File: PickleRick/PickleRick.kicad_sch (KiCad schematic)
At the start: 83 parts, among them J1 Conn_01x06_Male, J10 Conn_01x03_Male, J11 Conn_01x02_Male, J2 Conn_01x02_Male, J3 Conn_01x02_Male, J4 Micro_SD_Card_Det, J5 292227-7, Q1 MMDT2222A, Q2 PMV20ENR, U1 SN65HVD230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

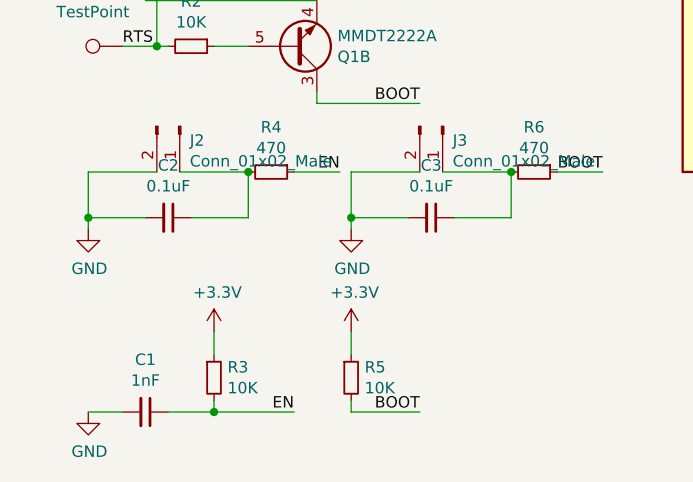
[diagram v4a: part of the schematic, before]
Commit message: changed autoprogrammer cap values
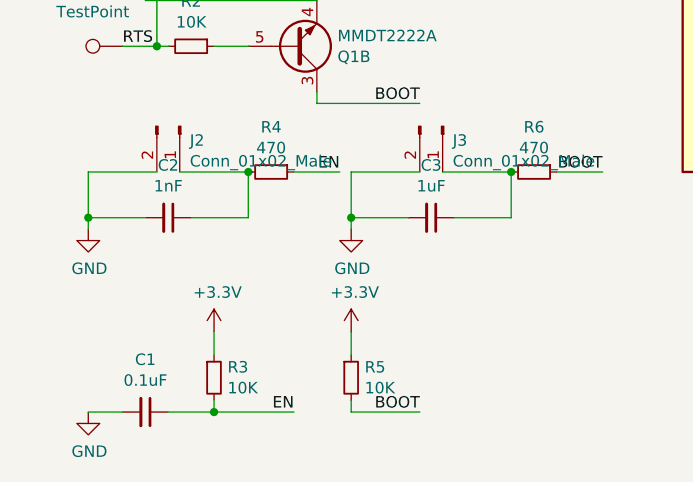
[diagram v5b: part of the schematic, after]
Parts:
- C1: value 1nF -> 0.1uF
- C2: value 0.1uF -> 1nF
- C3: value 0.1uF -> 1uF
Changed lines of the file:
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@@
     (in_bom yes) (on_board yes)
     (property "Reference" "C1" (id 0) (at 22.86 185.9534 90))
-    (property "Value" "1nF" (id 1) (at 22.86 188.2648 90))
+    (property "Value" "0.1uF" (id 1) (at 22.86 188.2648 90))
     (property "Footprint" "Capacitor_SMD:C_0603_1608Metric" (id 2) (at 22.86 191.77 0)
       (effects (font (size 1.27 1.27)) hide)
@@
     (in_bom yes) (on_board yes)
     (property "Reference" "C2" (id 0) (at 25.4 164.3634 90))
-    (property "Value" "0.1uF" (id 1) (at 25.4 166.6748 90))
+    (property "Value" "1nF" (id 1) (at 25.4 166.6748 90))
     (property "Footprint" "Capacitor_SMD:C_0603_1608Metric" (id 2) (at 25.4 170.18 0)
       (effects (font (size 1.27 1.27)) hide)
@@
     (in_bom yes) (on_board yes)
     (property "Reference" "C3" (id 0) (at 54.61 164.3634 90))
-    (property "Value" "0.1uF" (id 1) (at 54.61 166.6748 90))
+    (property "Value" "1uF" (id 1) (at 54.61 166.6748 90))
     (property "Footprint" "Capacitor_SMD:C_0603_1608Metric" (id 2) (at 54.61 170.18 0)
       (effects (font (size 1.27 1.27)) hide)
@@
     (path "/ca0eab8e-e3fd-464d-bb03-d1603b8a651b" (page "3"))
     (path "/7b7fe22f-5db7-4fb0-a6e2-91b9a8e5f484" (page "4"))
-    (path "/150d7a0e-7d8c-4788-bc30-4a3682bf4d09" (page "7"))
     (path "/53a382a5-9123-45f3-a2e9-3b2de6ca541d" (page "5"))
     (path "/698a410d-6a39-45b6-9e32-be9222181ad1" (page "7"))
+    (path "/150d7a0e-7d8c-4788-bc30-4a3682bf4d09" (page "7"))
     (path "/a5e505c0-c0af-4f61-a9d4-cf031c548012" (page "7"))
   )
@@
     )
     (path "/3bef0362-242d-46c4-b651-9d41a3c29516"
-      (reference "C1") (unit 1) (value "1nF") (footprint "Capacitor_SMD:C_0603_1608Metric")
+      (reference "C1") (unit 1) (value "0.1uF") (footprint "Capacitor_SMD:C_0603_1608Metric")
     )
     (path "/8f141cb6-d196-4940-89f8-4e8940598ec7"
-      (reference "C2") (unit 1) (value "0.1uF") (footprint "Capacitor_SMD:C_0603_1608Metric")
+      (reference "C2") (unit 1) (value "1nF") (footprint "Capacitor_SMD:C_0603_1608Metric")
     )
     (path "/d2eb360b-2bc4-4408-a8b3-07959277e262"
-      (reference "C3") (unit 1) (value "0.1uF") (footprint "Capacitor_SMD:C_0603_1608Metric")
+      (reference "C3") (unit 1) (value "1uF") (footprint "Capacitor_SMD:C_0603_1608Metric")
     )
     (path "/f238640e-3401-420a-ac31-a433f268cbfc"

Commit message: final changes to pick rick
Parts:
- C2: value 1nF -> 0.1uF
- C3: value 1uF -> 0.1uF
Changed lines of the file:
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@@
     (in_bom yes) (on_board yes)
     (property "Reference" "C2" (id 0) (at 25.4 164.3634 90))
-    (property "Value" "1nF" (id 1) (at 25.4 166.6748 90))
+    (property "Value" "0.1uF" (id 1) (at 25.4 166.6748 90))
     (property "Footprint" "Capacitor_SMD:C_0603_1608Metric" (id 2) (at 25.4 170.18 0)
       (effects (font (size 1.27 1.27)) hide)
@@
     (in_bom yes) (on_board yes)
     (property "Reference" "C3" (id 0) (at 54.61 164.3634 90))
-    (property "Value" "1uF" (id 1) (at 54.61 166.6748 90))
+    (property "Value" "0.1uF" (id 1) (at 54.61 166.6748 90))
     (property "Footprint" "Capacitor_SMD:C_0603_1608Metric" (id 2) (at 54.61 170.18 0)
       (effects (font (size 1.27 1.27)) hide)
@@
     (path "/ca0eab8e-e3fd-464d-bb03-d1603b8a651b" (page "3"))
     (path "/7b7fe22f-5db7-4fb0-a6e2-91b9a8e5f484" (page "4"))
+    (path "/150d7a0e-7d8c-4788-bc30-4a3682bf4d09" (page "7"))
     (path "/53a382a5-9123-45f3-a2e9-3b2de6ca541d" (page "5"))
     (path "/698a410d-6a39-45b6-9e32-be9222181ad1" (page "7"))
-    (path "/150d7a0e-7d8c-4788-bc30-4a3682bf4d09" (page "7"))
     (path "/a5e505c0-c0af-4f61-a9d4-cf031c548012" (page "7"))
   )
@@
     )
     (path "/8f141cb6-d196-4940-89f8-4e8940598ec7"
-      (reference "C2") (unit 1) (value "1nF") (footprint "Capacitor_SMD:C_0603_1608Metric")
+      (reference "C2") (unit 1) (value "0.1uF") (footprint "Capacitor_SMD:C_0603_1608Metric")
     )
     (path "/d2eb360b-2bc4-4408-a8b3-07959277e262"
-      (reference "C3") (unit 1) (value "1uF") (footprint "Capacitor_SMD:C_0603_1608Metric")
+      (reference "C3") (unit 1) (value "0.1uF") (footprint "Capacitor_SMD:C_0603_1608Metric")
     )
     (path "/f238640e-3401-420a-ac31-a433f268cbfc"

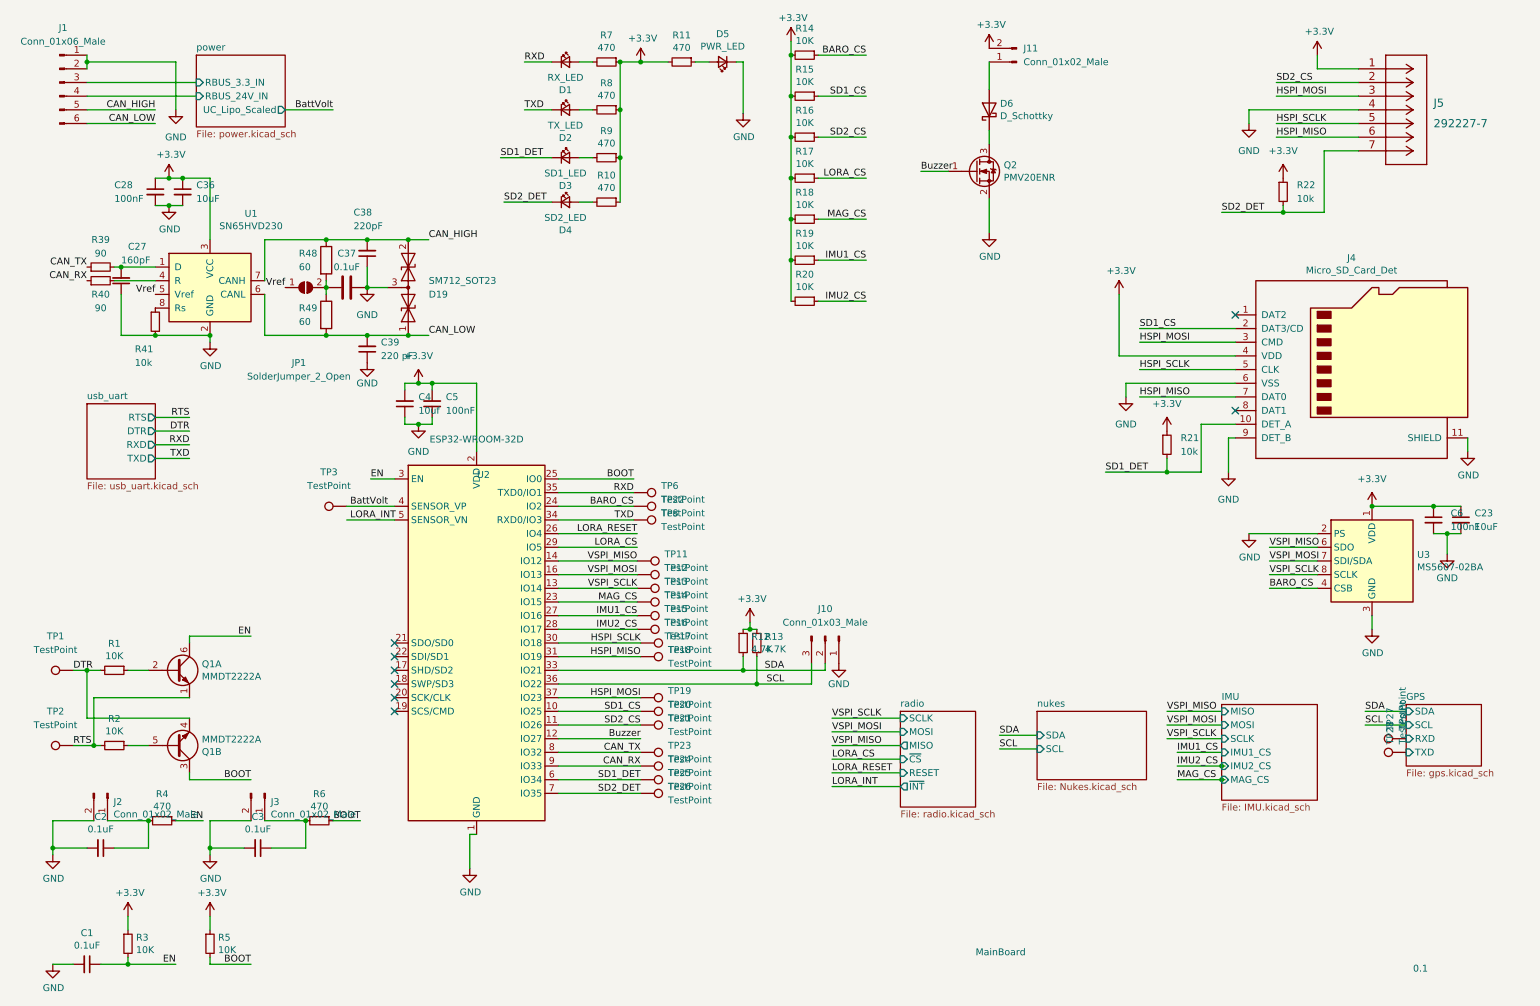
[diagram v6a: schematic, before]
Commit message: switched vspi and hspi labels so they are consistent with documentation
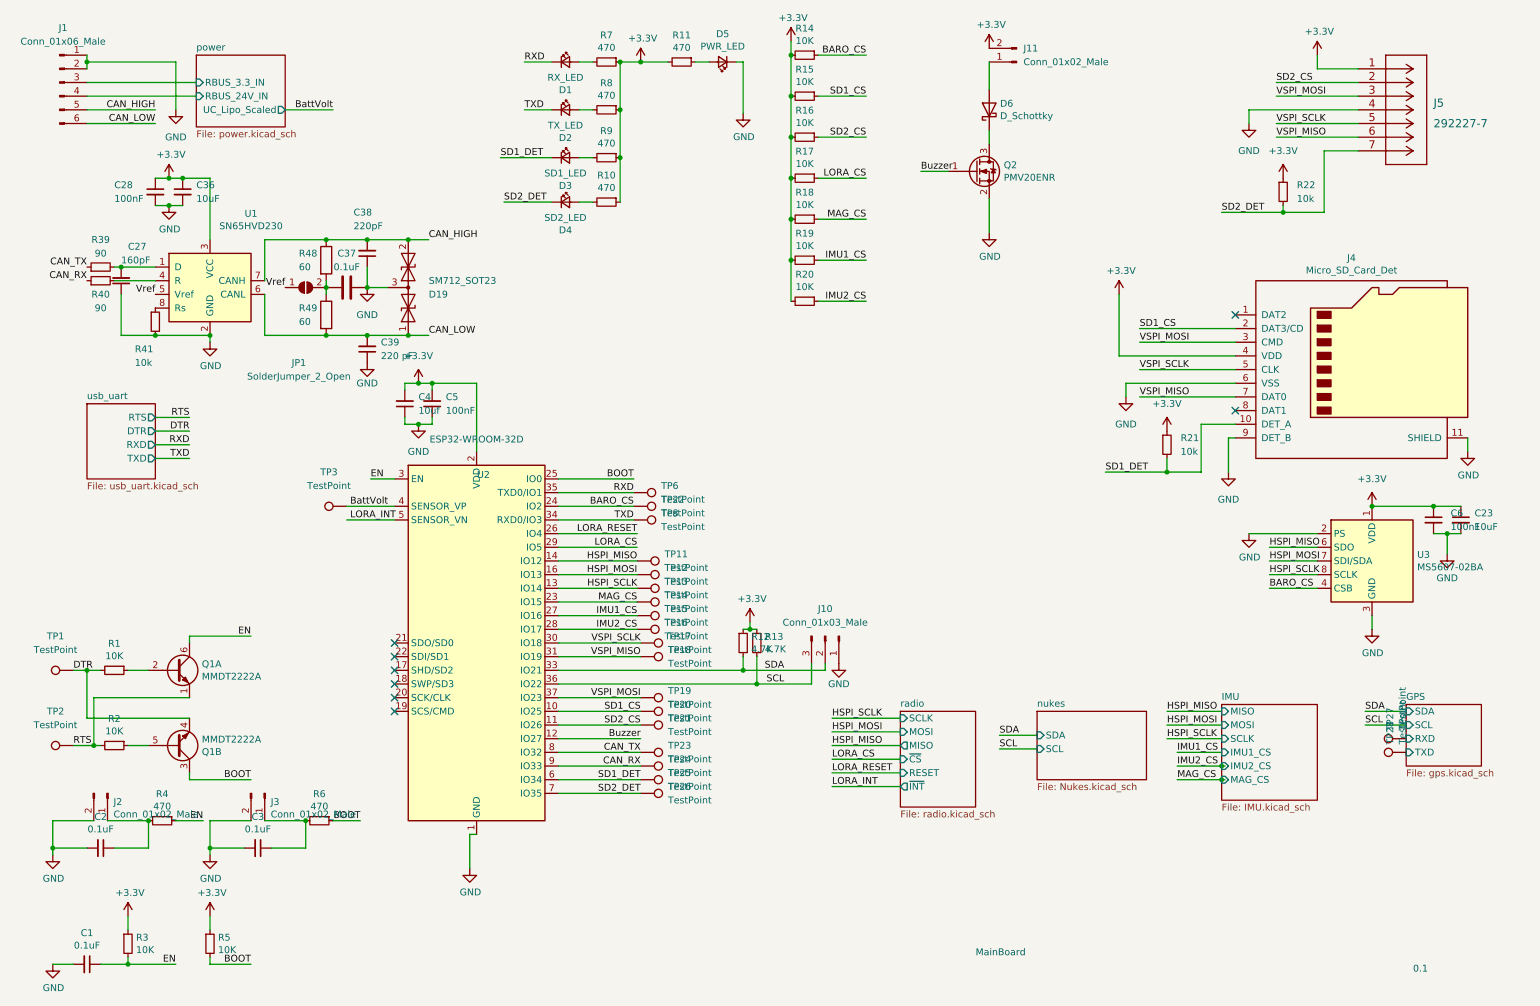
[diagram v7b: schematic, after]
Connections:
- net HSPI_MISO: now also TP11.1, U2.14 (IO12), U3.6 (SDO); no longer J4.7 (DAT0), J5.6, TP18.1, U2.31 (IO19)
- net HSPI_MOSI: now also TP12.1, U2.16 (IO13), U3.7 (SDI/SDA); no longer J4.3 (CMD), J5.3, TP19.1, U2.37 (IO23)
- net HSPI_SCLK: now also TP13.1, U2.13 (IO14), U3.8 (SCLK); no longer J4.5 (CLK), J5.5, TP17.1, U2.30 (IO18)
- net VSPI_MISO: now also J4.7 (DAT0), J5.6, TP18.1, U2.31 (IO19); no longer TP11.1, U2.14 (IO12), U3.6 (SDO)
- net VSPI_MOSI: now also J4.3 (CMD), J5.3, TP19.1, U2.37 (IO23); no longer TP12.1, U2.16 (IO13), U3.7 (SDI/SDA)
- net VSPI_SCLK: now also J4.5 (CLK), J5.5, TP17.1, U2.30 (IO18); no longer TP13.1, U2.13 (IO14), U3.8 (SCLK)
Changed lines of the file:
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@@
     (effects (font (size 1.27 1.27)) (justify left bottom))
   )
-  (label "VSPI_MOSI" (at 242.57 116.84 0)
+  (label "HSPI_MOSI" (at 242.57 116.84 0)
     (effects (font (size 1.27 1.27)) (justify left bottom))
   )
@@
     (effects (font (size 1.27 1.27)) (justify left bottom))
   )
-  (label "HSPI_MISO" (at 243.84 38.1 0)
+  (label "VSPI_MISO" (at 243.84 38.1 0)
     (effects (font (size 1.27 1.27)) (justify left bottom))
   )
@@
     (effects (font (size 1.27 1.27)) (justify left bottom))
   )
-  (label "VSPI_MISO" (at 161.29 151.13 0)
+  (label "HSPI_MISO" (at 161.29 151.13 0)
     (effects (font (size 1.27 1.27)) (justify left bottom))
   )
@@
     (effects (font (size 1.27 1.27)) (justify left bottom))
   )
-  (label "HSPI_MISO" (at 125.73 134.62 180)
+  (label "VSPI_MISO" (at 125.73 134.62 180)
     (effects (font (size 1.27 1.27)) (justify right bottom))
   )
@@
     (effects (font (size 1.27 1.27)) (justify right bottom))
   )
-  (label "HSPI_SCLK" (at 125.73 132.08 180)
+  (label "VSPI_SCLK" (at 125.73 132.08 180)
     (effects (font (size 1.27 1.27)) (justify right bottom))
   )
@@
     (effects (font (size 1.27 1.27)) (justify right bottom))
   )
-  (label "VSPI_MOSI" (at 161.29 148.59 0)
+  (label "HSPI_MOSI" (at 161.29 148.59 0)
     (effects (font (size 1.27 1.27)) (justify left bottom))
   )
@@
     (effects (font (size 1.27 1.27)) (justify right bottom))
   )
-  (label "VSPI_SCLK" (at 223.52 149.86 0)
+  (label "HSPI_SCLK" (at 223.52 149.86 0)
     (effects (font (size 1.27 1.27)) (justify left bottom))
   )
@@
     (effects (font (size 1.27 1.27)) (justify left bottom))
   )
-  (label "VSPI_SCLK" (at 161.29 146.05 0)
+  (label "HSPI_SCLK" (at 161.29 146.05 0)
     (effects (font (size 1.27 1.27)) (justify left bottom))
   )
@@
     (effects (font (size 1.27 1.27)) (justify right bottom))
   )
-  (label "VSPI_MISO" (at 223.52 144.78 0)
+  (label "HSPI_MISO" (at 223.52 144.78 0)
     (effects (font (size 1.27 1.27)) (justify left bottom))
   )
@@
     (effects (font (size 1.27 1.27)) (justify right bottom))
   )
-  (label "VSPI_MOSI" (at 223.52 147.32 0)
+  (label "HSPI_MOSI" (at 223.52 147.32 0)
     (effects (font (size 1.27 1.27)) (justify left bottom))
   )
@@
     (effects (font (size 1.27 1.27)) (justify left bottom))
   )
-  (label "VSPI_MISO" (at 242.57 114.3 0)
+  (label "HSPI_MISO" (at 242.57 114.3 0)
     (effects (font (size 1.27 1.27)) (justify left bottom))
   )
-  (label "VSPI_SCLK" (at 125.095 121.92 180)
+  (label "HSPI_SCLK" (at 125.095 121.92 180)
     (effects (font (size 1.27 1.27)) (justify right bottom))
   )
@@
     (effects (font (size 1.27 1.27)) (justify left bottom))
   )
-  (label "VSPI_SCLK" (at 242.57 119.38 0)
+  (label "HSPI_SCLK" (at 242.57 119.38 0)
     (effects (font (size 1.27 1.27)) (justify left bottom))
   )
@@
     (effects (font (size 1.27 1.27)) (justify left bottom))
   )
-  (label "HSPI_MISO" (at 218.44 86.36 0)
+  (label "VSPI_MISO" (at 218.44 86.36 0)
     (effects (font (size 1.27 1.27)) (justify left bottom))
   )
@@
     (effects (font (size 1.27 1.27)) (justify right bottom))
   )
-  (label "VSPI_MISO" (at 125.095 116.84 180)
+  (label "HSPI_MISO" (at 125.095 116.84 180)
     (effects (font (size 1.27 1.27)) (justify right bottom))
   )
@@
     (effects (font (size 1.27 1.27)) (justify left bottom))
   )
-  (label "HSPI_MOSI" (at 243.84 30.48 0)
+  (label "VSPI_MOSI" (at 243.84 30.48 0)
     (effects (font (size 1.27 1.27)) (justify left bottom))
   )
-  (label "HSPI_SCLK" (at 243.84 35.56 0)
+  (label "VSPI_SCLK" (at 243.84 35.56 0)
     (effects (font (size 1.27 1.27)) (justify left bottom))
   )
@@
     (effects (font (size 1.27 1.27)) (justify right bottom))
   )
-  (label "HSPI_MOSI" (at 125.73 142.24 180)
+  (label "VSPI_MOSI" (at 125.73 142.24 180)
     (effects (font (size 1.27 1.27)) (justify right bottom))
   )
-  (label "HSPI_SCLK" (at 218.44 81.28 0)
+  (label "VSPI_SCLK" (at 218.44 81.28 0)
     (effects (font (size 1.27 1.27)) (justify left bottom))
   )
@@
     (effects (font (size 1.27 1.27)) (justify left bottom))
   )
-  (label "VSPI_MOSI" (at 125.095 119.38 180)
+  (label "HSPI_MOSI" (at 125.095 119.38 180)
     (effects (font (size 1.27 1.27)) (justify right bottom))
   )
@@
     (effects (font (size 1.27 1.27)) (justify right bottom))
   )
-  (label "HSPI_MOSI" (at 218.44 76.2 0)
+  (label "VSPI_MOSI" (at 218.44 76.2 0)
     (effects (font (size 1.27 1.27)) (justify left bottom))
   )
@@
     )
     (path "/698a410d-6a39-45b6-9e32-be9222181ad1/310c0122-491e-42fa-affe-12d3fcc5ae04"
-      (reference "C30") (unit 1) (value "4.7uF") (footprint "Capacitor_SMD:CP_Elec_3x5.3")
+      (reference "C30") (unit 1) (value "4.7uF") (footprint "Capacitor_SMD:C_0603_1608Metric")
     )
     (path "/698a410d-6a39-45b6-9e32-be9222181ad1/4c5995c9-8ef2-4bc9-9217-6e626fe2bb82"
@@
     )
     (path "/7b7fe22f-5db7-4fb0-a6e2-91b9a8e5f484/b43f5fd2-756d-4ff4-a723-c4e592d5bb1a"
-      (reference "U7") (unit 1) (value "H3LIS100DLTR") (footprint "iclr:PQFN50P300X300X100-16N")
+      (reference "U7") (unit 1) (value "H3LIS331DLTR") (footprint "iclr:PQFN50P300X300X100-16N")
     )
     (path "/7b7fe22f-5db7-4fb0-a6e2-91b9a8e5f484/628ae615-b4c2-486e-899c-27441b67a16b"
